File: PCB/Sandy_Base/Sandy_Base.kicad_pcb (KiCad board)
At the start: 2 copper layers, 285 x 95.1 mm, 162 parts, among them J1 Conn_02x02_Top_Bottom, J10 Conn_01x03, J2 Conn_02x02_Top_Bottom, J3 Conn_02x02_Top_Bottom, J4 Conn_02x02_Top_Bottom, J5 Conn_02x02_Top_Bottom, J6 Conn_02x02_Top_Bottom, J7 USB_C_Receptacle_USB2.0, J8 Conn_02x03_Odd_Even, J9 Conn_01x02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

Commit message: ひととおりのソケットへの変更完了（プレートまだない）
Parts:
- REF**: footprint locallib:60_Outline-Sandy-Base5 -> locallib:60_Outline-Sandy-Base6
- SW_LSFT1u2: footprint MX_Alps_Hybrid:MXOnly-1U-Hotswap-guide -> MX_Alps_Hybrid:MXOnly-1U-Hotswap-custom5-guide
- SW_LSFT2u1: footprint MX_Alps_Hybrid:MXOnly-2U-Hotswap-ReversedStabilizers-guide2 -> MX_Alps_Hybrid:MXOnly-2U-Hotswap-ReversedStabilizers-guide2-custom11
- SW_RSPC1.5u1: footprint MX_Alps_Hybrid:MXOnly-1.5U-Hotswap-guide -> MX_Alps_Hybrid:MXOnly-1.5U-Hotswap-custom11-guide
- SW_RSPC2u1: footprint MX_Alps_Hybrid:MXOnly-2U-Hotswap-guide2 -> MX_Alps_Hybrid:MXOnly-2U-Hotswap-custom1-guide2
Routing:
- net RE_R2_1: track 252.6 -> 317.0 mm, vias 3 -> 7
- net Net-(D96-A): track 11.1 -> 38.7 mm, vias 0 -> 2
- net row9: track 329.3 -> 327.6 mm
- net RE_R1_1: track 342.0 -> 340.9 mm
- net RE_L_A: track 200.6 -> 201.3 mm
- net RE_L_B: track 199.3 -> 200.0 mm
- net Net-(D49-A): track 40.4 -> 41.0 mm
- net RE_R1_2: track 30.6 -> 31.2 mm
- net GND: vias 314 -> 313

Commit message: MId外形縮小
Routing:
- net LED: track 43.8 -> 53.4 mm, vias 1 -> 3
- net GND: track 72.0 -> 75.3 mm
- net MOSI: track 261.8 -> 259.0 mm
- net RE_L_A: track 201.3 -> 200.1 mm
- net Net-(LED2-DOUT): track 283.5 -> 284.6 mm
- net row4: track 341.4 -> 342.2 mm
- net SCK: track 289.5 -> 289.0 mm

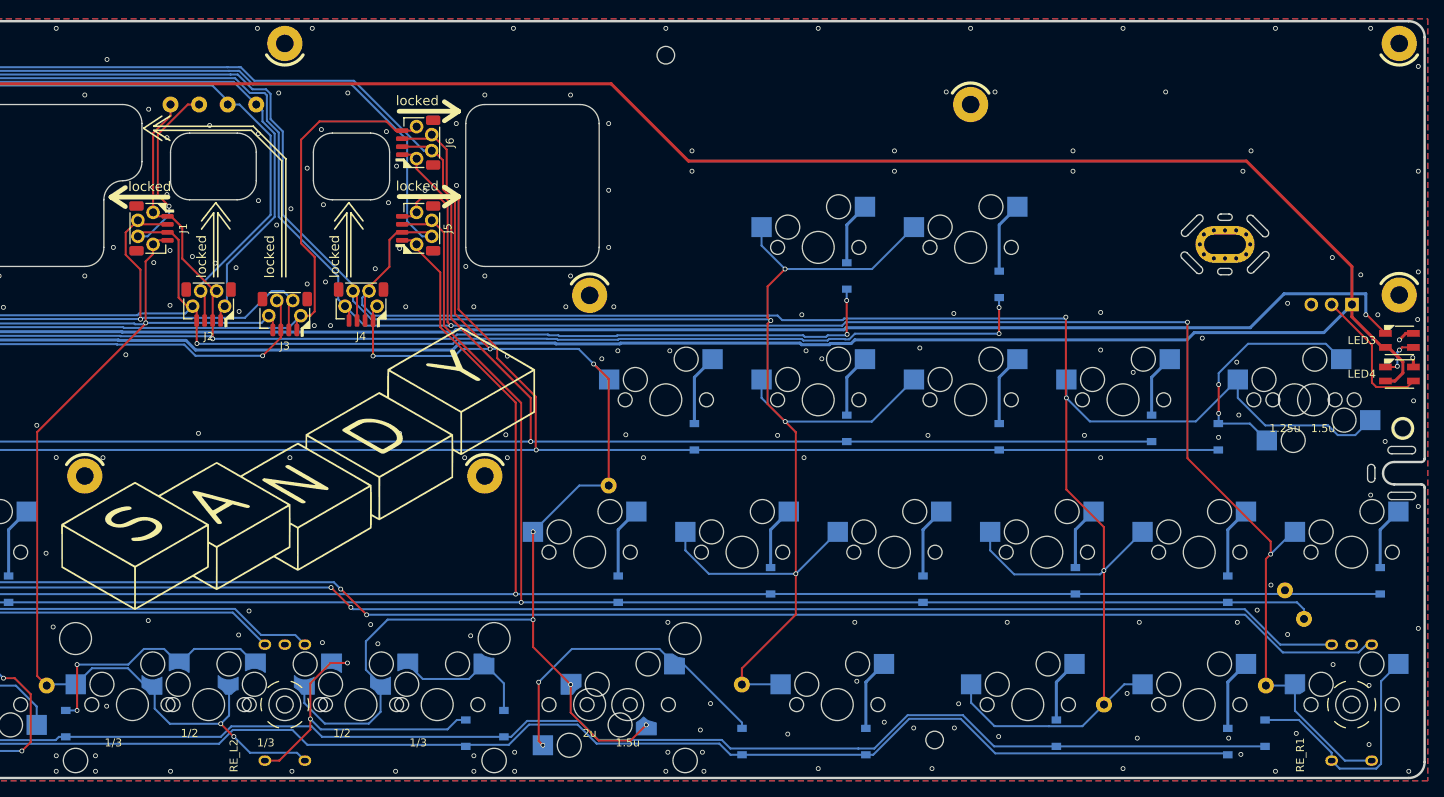
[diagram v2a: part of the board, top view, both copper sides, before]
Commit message: 各文字の位置がズレてるように見えるのを修正
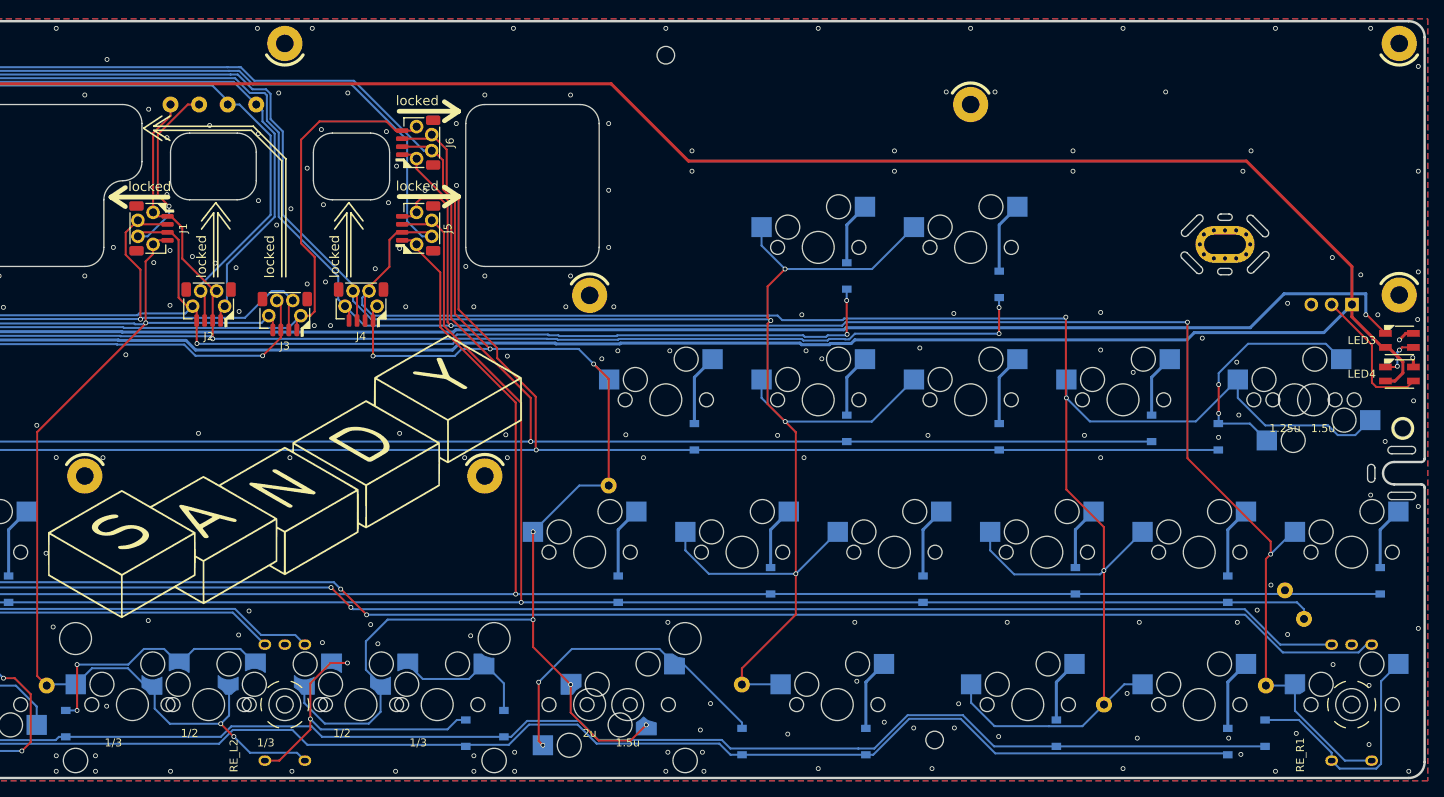
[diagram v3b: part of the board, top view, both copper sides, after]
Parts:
- removed LOGO1: Logo_Base, Jones.local:Sandy_logo_w60
- added G***: LOGO, Jones.local:Sandy_logo_w60_new, F.Cu at (159.2, 74.6)

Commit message: 微調整
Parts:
- removed the G*** at (159.2, 74.6)
- added LOGO1: Logo_Base, Jones.local:Sandy_logo_w60_new, F.Cu at (159.2, 73.4)
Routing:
- net RE_R2_1: track 317.0 -> 325.4 mm, vias 7 -> 6
- net Net-(LED2-DOUT): track 284.6 -> 279.6 mm
- net +5V: track 711.5 -> 715.8 mm, vias 13 -> 15
- net RE_L1_1: track 344.7 -> 343.1 mm
- net col5: track 335.7 -> 334.2 mm
- net row6: track 256.7 -> 255.6 mm
- net MISO: track 238.0 -> 238.9 mm
- net col6: track 406.3 -> 405.6 mm
- net SDA: track 43.1 -> 42.5 mm
- net SCL: track 43.3 -> 42.7 mm
- net row8: track 364.5 -> 365.1 mm
- net GND: vias 313 -> 312
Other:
- board text removed: "1.75u"
